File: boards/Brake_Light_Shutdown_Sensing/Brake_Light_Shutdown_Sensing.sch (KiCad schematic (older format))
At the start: 85 parts, among them IC1 ATMEGA16M1, J1 micromatch_female_RA_10, J2 micromatch_female_RA_20, P1 CONN_02X03, Q1 SSM3K333R, Q2 SSM3K333R, Q3 SSM3K333R, Q4 SSM3K333R, Q5 SSM3K333R, Q6 SSM3K333R, Q7 SSM3K333R, U1 MCP6001RT, U2 TPS561201, U3 CP2120, U4 LM1117-1.8, U5 CAN_Transceiver, Y1 Crystal_SMD

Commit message: Updated schematic with Atmega 16 instead of cp2120
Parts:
- removed C11: C_0.1uF, footprints:C_0805_OEM, symbol C_0.1uF
- removed C9: C_0.1uF, footprints:C_0805_OEM, symbol C_10uF
- removed D12: LED_0805, footprints:LED_0805_OEM, symbol LED_0805
- removed J1: micromatch_female_RA_10, footprints:micromatch_female_ra_10, symbol micromatch_female_RA_10
- removed R32, R36, R37: 4.7K, footprints:R_0805_OEM, symbol R
- removed R33, R34, R35, R40, R41: R_1k, footprints:R_0805_OEM, symbol R_1k
- removed U3: CP2120, footprints:CP2120-QFN, symbol CP2120
- removed U4: LM1117-1.8, TO_SOT_Packages_SMD:SOT-223, symbol LM1117-1.8
- added C11, C9: C_30pF, footprints:C_0805_OEM, symbol C_30pF
- added J1: micromatch_female_RA_6, footprints:micromatch_female_ra_6, symbol micromatch_female_RA_6
- added P2: CONN_02X03, footprints:Pin_Header_Straight_2x03, symbol CONN_02X03
- added R32, R33, R34, R35: R_200, footprints:R_0805_OEM, symbol R_200
- added R36, R37: R_10k, footprints:R_0805_OEM, symbol R_10k
- added U3: ATMEGA328P-AU, Housings_QFP:TQFP-32_7x7mm_Pitch0.8mm, symbol ATMEGA328P-AU
- added Y2: Crystal_SMD, footprints:Crystal_SMD_FA238, symbol Crystal_SMD
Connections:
- net labels added: LED5, LED6, RST32, XTAL1, XTAL2, data1, data2, data3, data4
- net labels removed: +3.3V, 3.3V, Analog_Brake+, Analog_Brake-, CS, EINT, GPIO_O, INT, RST
- no-connect marks 18 -> 19
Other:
- note added: "Atmega 16 (Main Microcontroller)"
- note added: "Atmega 32"
- note added: "Brake Light Circuit"
- note added: "Buck Converter"
- note added: "Shut Down Sensing"
- moved on the sheet: C1, C10, C2, C3, C4, C5, C6, C8, D1, D13, D14, D2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

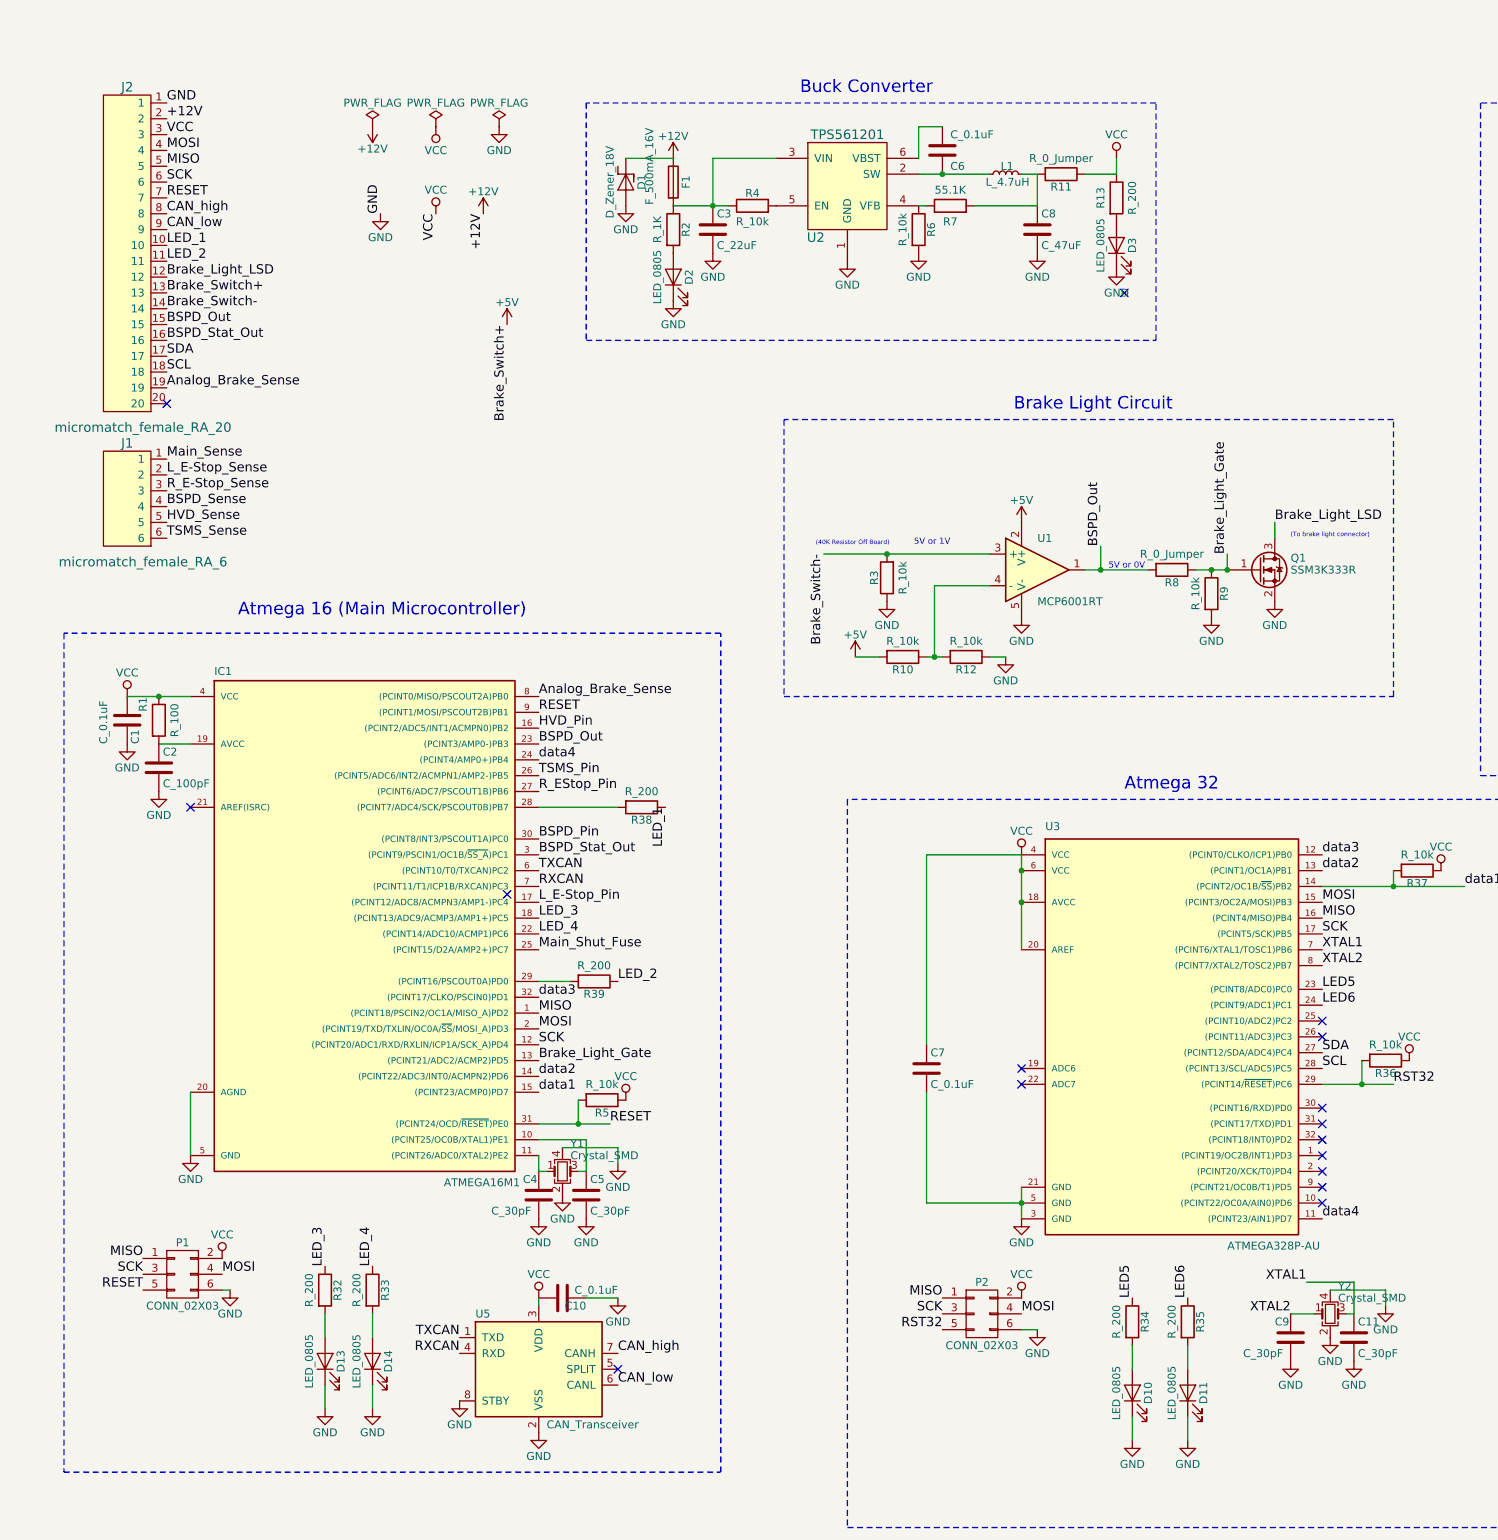
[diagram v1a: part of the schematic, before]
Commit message: Updated Layout (added bypass cap to Brake Light Circuit), continued with layout, and started tracing modules
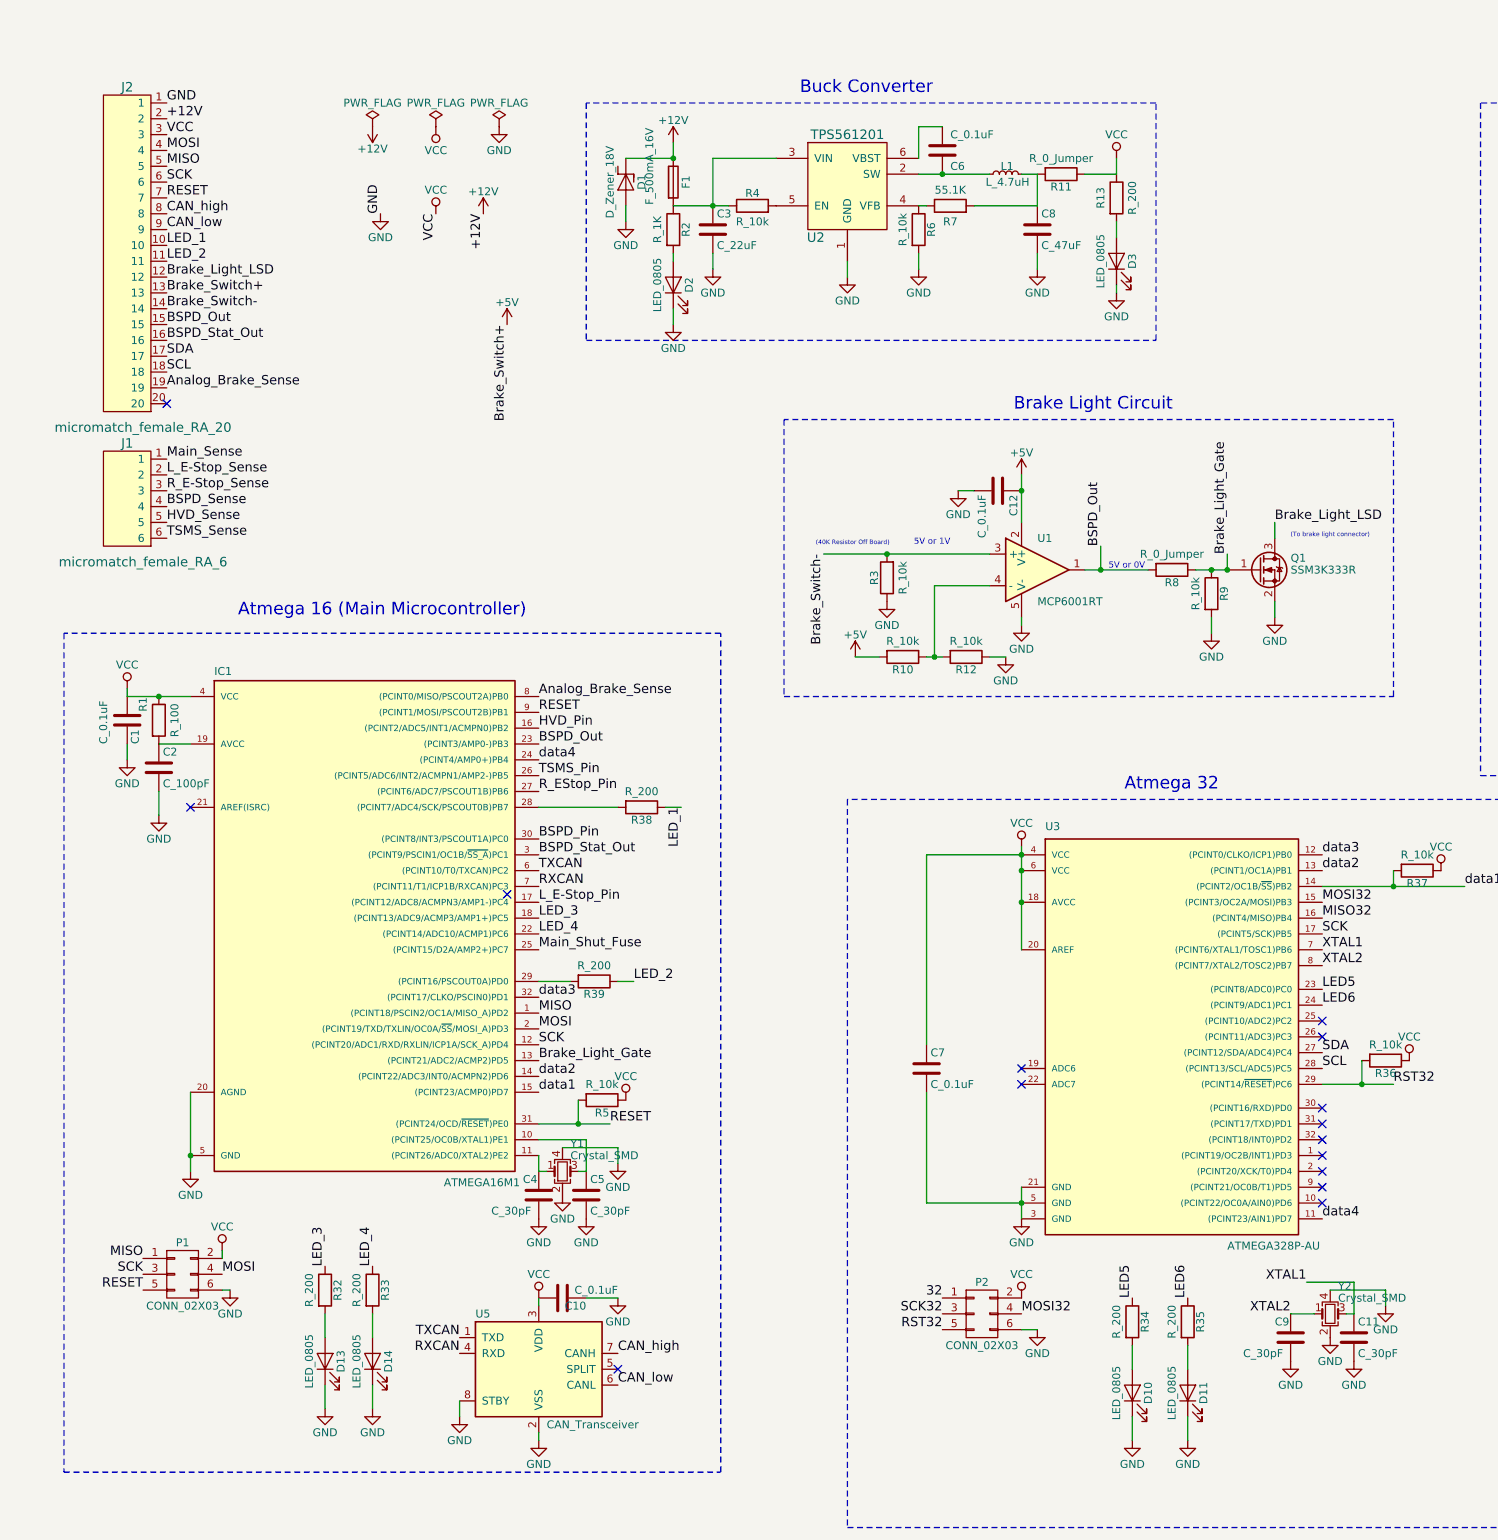
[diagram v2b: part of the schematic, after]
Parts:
- added C12: C_0.1uF, footprints:C_0805_OEM, symbol C_0.1uF
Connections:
- net +5V: now also C12.1
- net GND: now also C12.2
- net MISO: no longer P2.1 (P1), U3.16 ((PCINT4/MISO)PB4)
- net MOSI: no longer P2.4 (P4), U3.15 ((PCINT3/OC2A/MOSI)PB3)
- net SCK: no longer P2.3 (P3)
- new net 32: P2.1 (P1)
- new net MISO32: U3.16 ((PCINT4/MISO)PB4)
- new net MOSI32: P2.4 (P4), U3.15 ((PCINT3/OC2A/MOSI)PB3)
- new net SCK32: P2.3 (P3)
- no-connect marks 19 -> 18
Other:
- moved on the sheet: D2, D3

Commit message: Updated Layout
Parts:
- added C13: C_1uF, footprints:C_0805_OEM, symbol C_1uF
- added C14: C_0.1uF, footprints:C_0805_OEM, symbol C_0.1uF
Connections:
- net 32 is gone; now on net MISO: P2.1 (P1)
- net MISO32 is gone; now on net MISO: U3.16 ((PCINT4/MISO)PB4)
- net MOSI32 is gone; now on net MOSI: P2.4 (P4), U3.15 ((PCINT3/OC2A/MOSI)PB3)
- net SCK32 is gone; now on net SCK: P2.3 (P3)
- net +5V: now also J2.11; no longer J2.13
- net Analog_Brake_Sense: now also IC1.28 ((PCINT7/ADC4/SCK/PSCOUT0B)PB7), J2.14; no longer IC1.8 ((PCINT0/MISO/PSCOUT2A)PB0), J2.19
- net BSPD_Out: now also IC1.27 ((PCINT6/ADC7/PSCOUT1B)PB6), J2.13; no longer IC1.23 ((PCINT3/AMP0-)PB3), J2.15
- net BSPD_Pin: now also IC1.14 ((PCINT22/ADC3/INT0/ACMPN2)PD6); no longer IC1.30 ((PCINT8/INT3/PSCOUT1A)PC0)
- net BSPD_Stat_Out: now also J2.17; no longer J2.16
- net Brake_Light_Gate: now also IC1.26 ((PCINT5/ADC6/INT2/ACMPN1/AMP2-)PB5); no longer IC1.13 ((PCINT21/ADC2/ACMP2)PD5)
- net Brake_Light_LSD: now also J2.10; no longer J2.12
- net Brake_Switch-: now also J2.12; no longer J2.14
- net GND: now also C13.2, C14.2
- net HVD_Pin: now also IC1.15 ((PCINT23/ACMP0)PD7); no longer IC1.16 ((PCINT2/ADC5/INT1/ACMPN0)PB2)
- net LED_1: now also J2.15, R39.1; no longer J2.10, R38.1
- net LED_2: now also J2.16, R38.1; no longer J2.11, R39.1
- net LED_4: now also IC1.17 ((PCINT12/ADC8/ACMPN3/AMP1-)PC4); no longer IC1.22 ((PCINT14/ADC10/ACMP1)PC6)
- net L_E-Stop_Pin: now also IC1.9 ((PCINT1/MOSI/PSCOUT2B)PB1); no longer IC1.17 ((PCINT12/ADC8/ACMPN3/AMP1-)PC4)
- net Main_Shut_Fuse: now also IC1.8 ((PCINT0/MISO/PSCOUT2A)PB0); no longer IC1.25 ((PCINT15/D2A/AMP2+)PC7)
- net RESET: no longer IC1.9 ((PCINT1/MOSI/PSCOUT2B)PB1)
- net R_EStop_Pin: now also IC1.13 ((PCINT21/ADC2/ACMP2)PD5); no longer IC1.27 ((PCINT6/ADC7/PSCOUT1B)PB6)
- net SCL: now also J2.19; no longer J2.18
- net SDA: now also J2.18; no longer J2.17
- net TSMS_Pin: now also IC1.16 ((PCINT2/ADC5/INT1/ACMPN0)PB2); no longer IC1.26 ((PCINT5/ADC6/INT2/ACMPN1/AMP2-)PB5)
- net data1: now also IC1.22 ((PCINT14/ADC10/ACMP1)PC6); no longer IC1.15 ((PCINT23/ACMP0)PD7)
- net data2: now also IC1.23 ((PCINT3/AMP0-)PB3); no longer IC1.14 ((PCINT22/ADC3/INT0/ACMPN2)PD6)
- net data3: now also IC1.24 ((PCINT4/AMP0+)PB4); no longer IC1.32 ((PCINT17/CLKO/PSCIN0)PD1)
- net data4: now also IC1.25 ((PCINT15/D2A/AMP2+)PC7); no longer IC1.24 ((PCINT4/AMP0+)PB4)
- net at C8.1, L1.2, R11.2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: now also C13.1, C14.1
- net at R38.2: now also IC1.30 ((PCINT8/INT3/PSCOUT1A)PC0); no longer IC1.28 ((PCINT7/ADC4/SCK/PSCOUT0B)PB7)
- no-connect marks 18 -> 17
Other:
- moved on the sheet: R38
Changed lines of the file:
@@
-$EndComp
-$Comp
-L ATMEGA16M1 IC1
-U 1 1 59E10948
-P 2600 6250
-F 0 "IC1" H 1650 8080 50  0000 L BNN
-F 1 "ATMEGA16M1" H 3100 4850 50  0000 L BNN
-F 2 "footprints:TQFP-32_7x7mm_Pitch0.8mm" H 2600 6250 50  0001 C CIN
-F 3 "http://www.atmel.com/Images/Atmel-8209-8-bit%20AVR%20ATmega16M1-32M1-64M1_Datasheet.pdf" H 1650 8080 50  0001 C CNN
-F 4 "ATMEGA16M1-AU-ND" H 2600 6250 60  0001 C CNN "MPN"
-F 5 "Digi-Key" H 2600 6250 60  0001 C CNN "MFN"
-F 6 "Value" H 2600 6250 60  0001 C CNN "Package"
-F 7 "https://www.digikey.com/product-detail/en/atmel/ATMEGA16M1-AU/ATMEGA16M1-AU-ND/2271208" H 2050 8480 60  0001 C CNN "PurchasingLink"
-	1    2600 6250
-	1    0    0    -1
 $EndComp
 $Comp
@@
 Text Label 14300 1400 0    59   ~ 0
 L_E-Stop_Pin
-Text Label 3700 5850 0    59   ~ 0
+Text Label 3700 4650 0    59   ~ 0
 L_E-Stop_Pin
 Text Label 12750 1400 0    59   ~ 0
@@
 Text Label 1350 900  0    59   ~ 0
 +12V
-Text Label 1350 1900 0    59   ~ 0
+Text Label 1350 1700 0    59   ~ 0
 Brake_Light_LSD
 Text Label 1350 1000 0    59   ~ 0
@@
 Text Label 3700 5550 0    59   ~ 0
 BSPD_Stat_Out
-Text Label 1350 2300 0    59   ~ 0
+Text Label 1350 2400 0    59   ~ 0
 BSPD_Stat_Out
 Text Label 1350 3250 0    59   ~ 0
@@
 Text Label 1350 3450 0    59   ~ 0
 HVD_Sense
-Text Label 1350 2400 0    59   ~ 0
+Text Label 1350 2500 0    59   ~ 0
 SDA
-Text Label 1350 2500 0    59   ~ 0
+Text Label 1350 2600 0    59   ~ 0
 SCL
+Text Label 3700 5050 0    59   ~ 0
+Brake_Light_Gate
+Text Label 3700 7050 0    59   ~ 0
+HVD_Pin
 Text Label 3700 6850 0    59   ~ 0
-Brake_Light_Gate
+R_EStop_Pin
 Text Label 3700 4750 0    59   ~ 0
-HVD_Pin
-Text Label 3700 5150 0    59   ~ 0
-R_EStop_Pin
-Text Label 3700 5050 0    59   ~ 0
 TSMS_Pin
-Text Label 3700 6150 0    59   ~ 0
+Text Label 3700 4550 0    59   ~ 0
 Main_Shut_Fuse
-Text Label 3700 5450 0    59   ~ 0
+Text Label 3700 6950 0    59   ~ 0
 BSPD_Pin
-NoConn ~ 3500 5800
 NoConn ~ 10600 1650
-NoConn ~ -4650 -900
 NoConn ~ 10400 3600
-Text Label 1350 1700 0    59   ~ 0
+Text Label 1350 2200 0    59   ~ 0
 LED_1
-Text Label 1350 1800 0    59   ~ 0
+Text Label 1350 2300 0    59   ~ 0
 LED_2
 $Comp
 L R_200 R38
 U 1 1 5A303208
-P 4350 5250
-F 0 "R38" V 4430 5250 50  0000 C CNN
-F 1 "R_200" V 4250 5250 50  0000 C CNN
-F 2 "footprints:R_0805_OEM" H 4280 5250 50  0001 C CNN
-F 3 "https://www.seielect.com/Catalog/SEI-RMCF_RMCP.pdf" H 4430 5250 50  0001 C CNN
-F 4 "Digi-Key" H 4350 5250 60  0001 C CNN "MFN"
-F 5 "RMCF0805JT200RCT-ND" H 4350 5250 60  0001 C CNN "MPN"
-F 6 "Value" H 4350 5250 60  0001 C CNN "Package"
-F 7 "https://www.digikey.com/products/en?keywords=RMCF0805JT200RCT-ND" H 4830 5650 60  0001 C CNN "PurchasingLink"
-	1    4350 5250
+P 4600 5450
+F 0 "R38" V 4680 5450 50  0000 C CNN
+F 1 "R_200" V 4500 5450 50  0000 C CNN
+F 2 "footprints:R_0805_OEM" H 4530 5450 50  0001 C CNN
+F 3 "https://www.seielect.com/Catalog/SEI-RMCF_RMCP.pdf" H 4680 5450 50  0001 C CNN
+F 4 "Digi-Key" H 4600 5450 60  0001 C CNN "MFN"
+F 5 "RMCF0805JT200RCT-ND" H 4600 5450 60  0001 C CNN "MPN"
+F 6 "Value" H 4600 5450 60  0001 C CNN "Package"
+F 7 "https://www.digikey.com/products/en?keywords=RMCF0805JT200RCT-ND" H 5080 5850 60  0001 C CNN "PurchasingLink"
+	1    4600 5450
 	0    1    1    0
 $EndComp
@@
 	0    1    1    0
 $EndComp
-Text Label 4600 5250 3    59   ~ 0
+Text Label 4300 6350 0    59   ~ 0
 LED_1
-Text Label 4300 6350 0    59   ~ 0
+Text Label 4850 5450 0    59   ~ 0
 LED_2
 $Comp
@@
 Text Label 3700 5950 0    59   ~ 0
 LED_3
-Text Label 3700 6050 0    59   ~ 0
+Text Label 3700 5850 0    59   ~ 0
 LED_4
 $Comp
@@
 	-1   0    0    1
 $EndComp
-Text Label 1350 2600 0    59   ~ 0
+Text Label 1350 2100 0    59   ~ 0
 Analog_Brake_Sense
+Text Label 1350 1800 0    59   ~ 0
+Brake_Switch+
+Text Label 1350 1900 0    59   ~ 0
+Brake_Switch-
 Text Label 1350 2000 0    59   ~ 0
-Brake_Switch+
-Text Label 1350 2100 0    59   ~ 0
-Brake_Switch-
-Text Label 1350 2200 0    59   ~ 0
 BSPD_Out
 Text Label 1350 3050 0    59   ~ 0
@@
 	1    0    0    -1
 $EndComp
-Text Label 3700 4550 0    59   ~ 0
+Text Label 3700 5250 0    59   ~ 0
 Analog_Brake_Sense
-Text Label 3700 4650 0    59   ~ 0
-RESET
-Text Label 3700 4850 0    59   ~ 0
+Text Label 3700 5150 0    59   ~ 0
 BSPD_Out
 $Comp
@@
 $EndComp
 Text Label 6250 8350 2    59   ~ 0
-32
+MISO
 Text Label 6250 8450 2    59   ~ 0
-SCK32
+SCK
 $Comp
 L VCC #PWR069
@@
 $EndComp
 Text Label 6750 8450 0    59   ~ 0
-MOSI32
+MOSI
 $Comp
 L GND #PWR070
@@
 RST32
 Text Label 8650 5850 0    59   ~ 0
-MOSI32
+MOSI
 Text Label 8650 5950 0    59   ~ 0
-MISO32
+MISO
 Text Label 8650 6050 0    59   ~ 0
 SCK
@@
 Text Label 9550 5750 0    59   ~ 0
 data1
-Text Label 3700 7050 0    59   ~ 0
+Text Label 3700 6050 0    59   ~ 0
 data1
-Text Label 3700 6950 0    59   ~ 0
+Text Label 3700 4850 0    59   ~ 0
 data2
 Text Label 8650 5650 0    59   ~ 0
@@
 Text Label 8650 7850 0    59   ~ 0
 data4
-Text Label 3700 6450 0    59   ~ 0
+Text Label 3700 4950 0    59   ~ 0
 data3
-Text Label 3700 4950 0    59   ~ 0
+Text Label 3700 6150 0    59   ~ 0
 data4
 Text Label 8650 6400 0    59   ~ 0
@@
 	2650 9050 2650 8900
 Wire Wire Line
-	3700 5250 4200 5250
-Wire Wire Line
 	3700 6350 3900 6350
-Wire Wire Line
-	6750 5500 6750 6150
 Connection ~ 6750 5650
 Connection ~ 6750 5850
@@
 	1100 4500 1100 4550
 Wire Wire Line
-	4500 5250 4600 5250
+	4750 5450 4850 5450
 Wire Wire Line
 	4200 6350 4300 6350
@@
 	1700 8050 1700 8100
 Connection ~ 1500 7450
+$Comp
+L C_0.1uF C14
+U 1 1 5A8226BF
+P 6650 1600
+F 0 "C14" H 6675 1700 50  0000 L CNN
+F 1 "C_0.1uF" H 6675 1500 50  0000 L CNN
+F 2 "footprints:C_0805_OEM" H 6688 1450 50  0001 C CNN
+F 3 "http://datasheets.avx.com/X7RDielectric.pdf" H 6675 1700 50  0001 C CNN
+F 4 "478-3352-1-ND" H 6650 1600 60  0001 C CNN "MPN"
+F 5 "Digi-Key" H 6650 1600 60  0001 C CNN "MFN"
+F 6 "Value" H 6650 1600 60  0001 C CNN "Package"
+F 7 "https://www.digikey.com/products/en?keywords=478-3352-1-ND" H 7075 2100 60  0001 C CNN "PurchasingLink"
+	1    6650 1600
+	1    0    0    -1
+$EndComp
+$Comp
+L C_1uF C13
+U 1 1 5A8227BA
+P 6450 1600
+F 0 "C13" H 6475 1700 50  0000 L CNN
+F 1 "C_1uF" H 6475 1500 50  0000 L CNN
+F 2 "footprints:C_0805_OEM" H 6488 1450 50  0001 C CNN
+F 3 "http://datasheets.avx.com/X7RDielectric.pdf" H 6475 1700 50  0001 C CNN
+F 4 "CAP CER 1UF 25V X7R 0805" H 6975 2200 60  0001 C CNN "Description"
+F 5 "478-10487-1-ND" H 6450 1600 60  0001 C CNN "MPN"
+F 6 "Digi-Key" H 6450 1600 60  0001 C CNN "MFN"
+F 7 "Value" H 6450 1600 60  0001 C CNN "Package"
+F 8 "https://www.digikey.com/product-detail/en/avx-corporation/08053C105JAT2A/478-10487-1-ND/6797628" H 6875 2100 60  0001 C CNN "PurchasingLink"
+	1    6450 1600
+	1    0    0    -1
+$EndComp
+$Comp
+L GND #PWR075
+U 1 1 5A822FDC
+P 6450 1750
+F 0 "#PWR075" H 6450 1500 50  0001 C CNN
+F 1 "GND" H 6450 1600 50  0000 C CNN
+F 2 "" H 6450 1750 50  0001 C CNN
+F 3 "" H 6450 1750 50  0001 C CNN
+	1    6450 1750
+	1    0    0    -1
+$EndComp
+$Comp
+L GND #PWR076
+U 1 1 5A82309C
+P 6650 1750
+F 0 "#PWR076" H 6650 1500 50  0001 C CNN
+F 1 "GND" H 6650 1600 50  0000 C CNN
+F 2 "" H 6650 1750 50  0001 C CNN
+F 3 "" H 6650 1750 50  0001 C CNN
+	1    6650 1750
+	1    0    0    -1
+$EndComp
+Connection ~ 6650 1450
+Connection ~ 8850 8350
+Wire Wire Line
+	6750 5500 6750 6150
+$Comp
+L ATMEGA16M1 IC1
+U 1 1 59E10948
+P 2600 6250
+F 0 "IC1" H 1650 8080 50  0000 L BNN
+F 1 "ATMEGA16M1" H 3100 4850 50  0000 L BNN
+F 2 "footprints:TQFP-32_7x7mm_Pitch0.8mm" H 2600 6250 50  0001 C CIN
+F 3 "http://www.atmel.com/Images/Atmel-8209-8-bit%20AVR%20ATmega16M1-32M1-64M1_Datasheet.pdf" H 1650 8080 50  0001 C CNN
+F 4 "ATMEGA16M1-AU-ND" H 2600 6250 60  0001 C CNN "MPN"
+F 5 "Digi-Key" H 2600 6250 60  0001 C CNN "MFN"
+F 6 "Value" H 2600 6250 60  0001 C CNN "Package"
+F 7 "https://www.digikey.com/product-detail/en/atmel/ATMEGA16M1-AU/ATMEGA16M1-AU-ND/2271208" H 2050 8480 60  0001 C CNN "PurchasingLink"
+	1    2600 6250
+	1    0    0    -1
+$EndComp
+Wire Wire Line
+	3700 5450 4450 5450
+NoConn ~ 3700 6450
 $EndSCHEMATC
